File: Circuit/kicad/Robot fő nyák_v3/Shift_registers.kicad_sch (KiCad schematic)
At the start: 2 parts, among them U54 MCP23S17_SO, U55 MCP23S17_SO

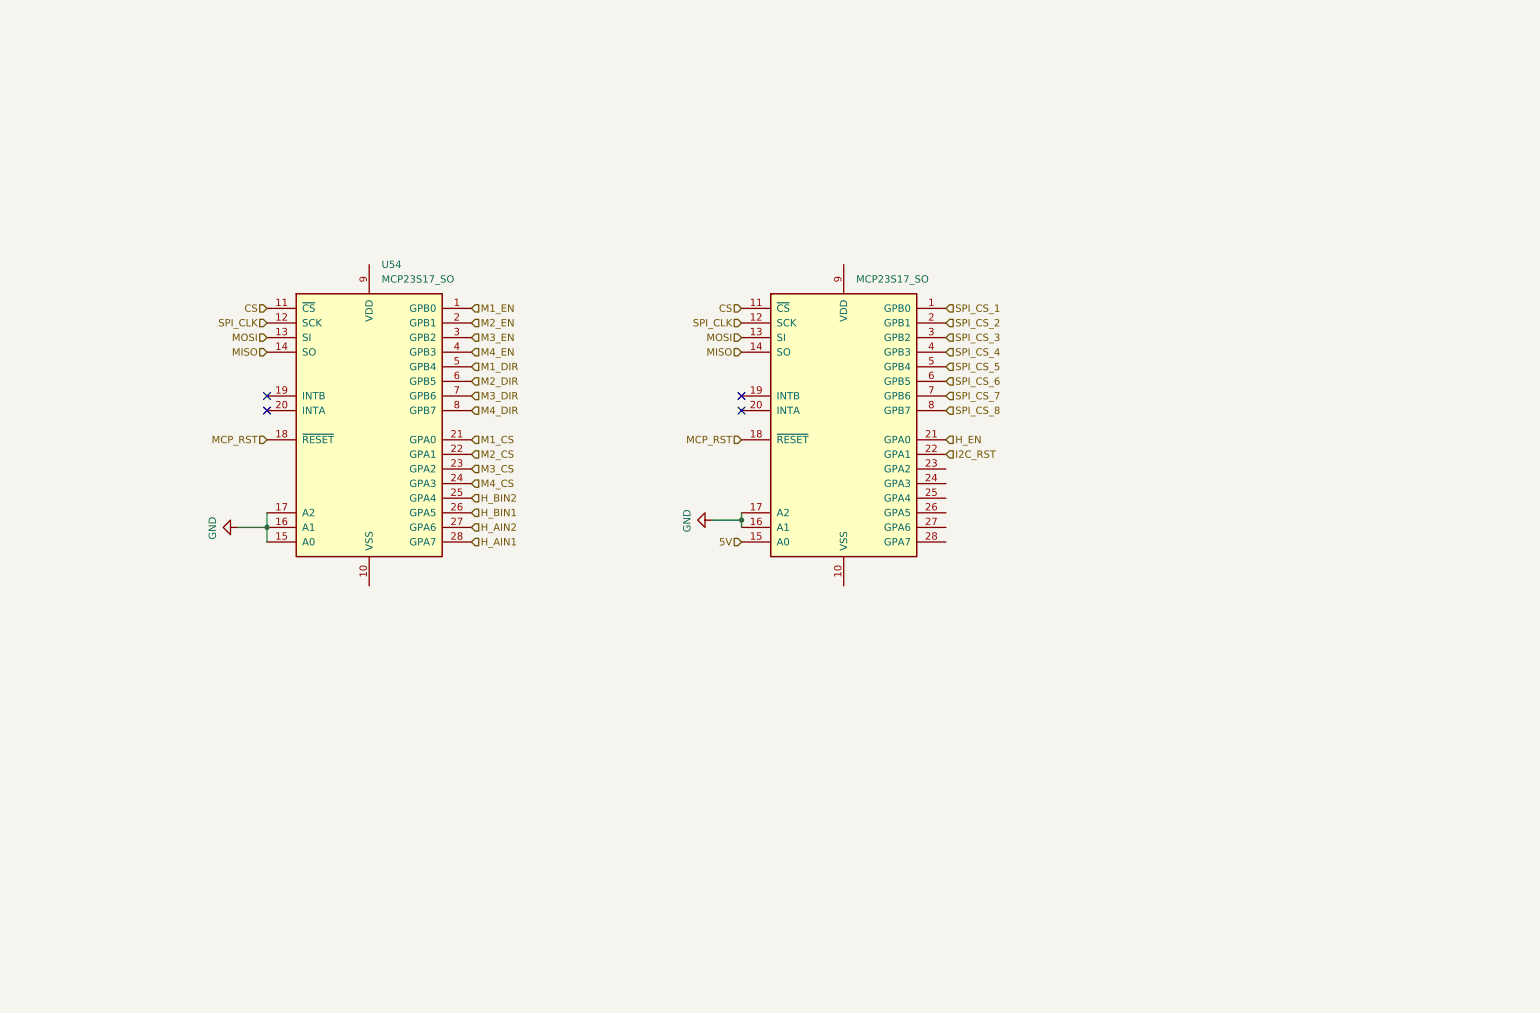
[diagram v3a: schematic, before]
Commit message: kicad  i2c and spi mux fixed and bugfixs
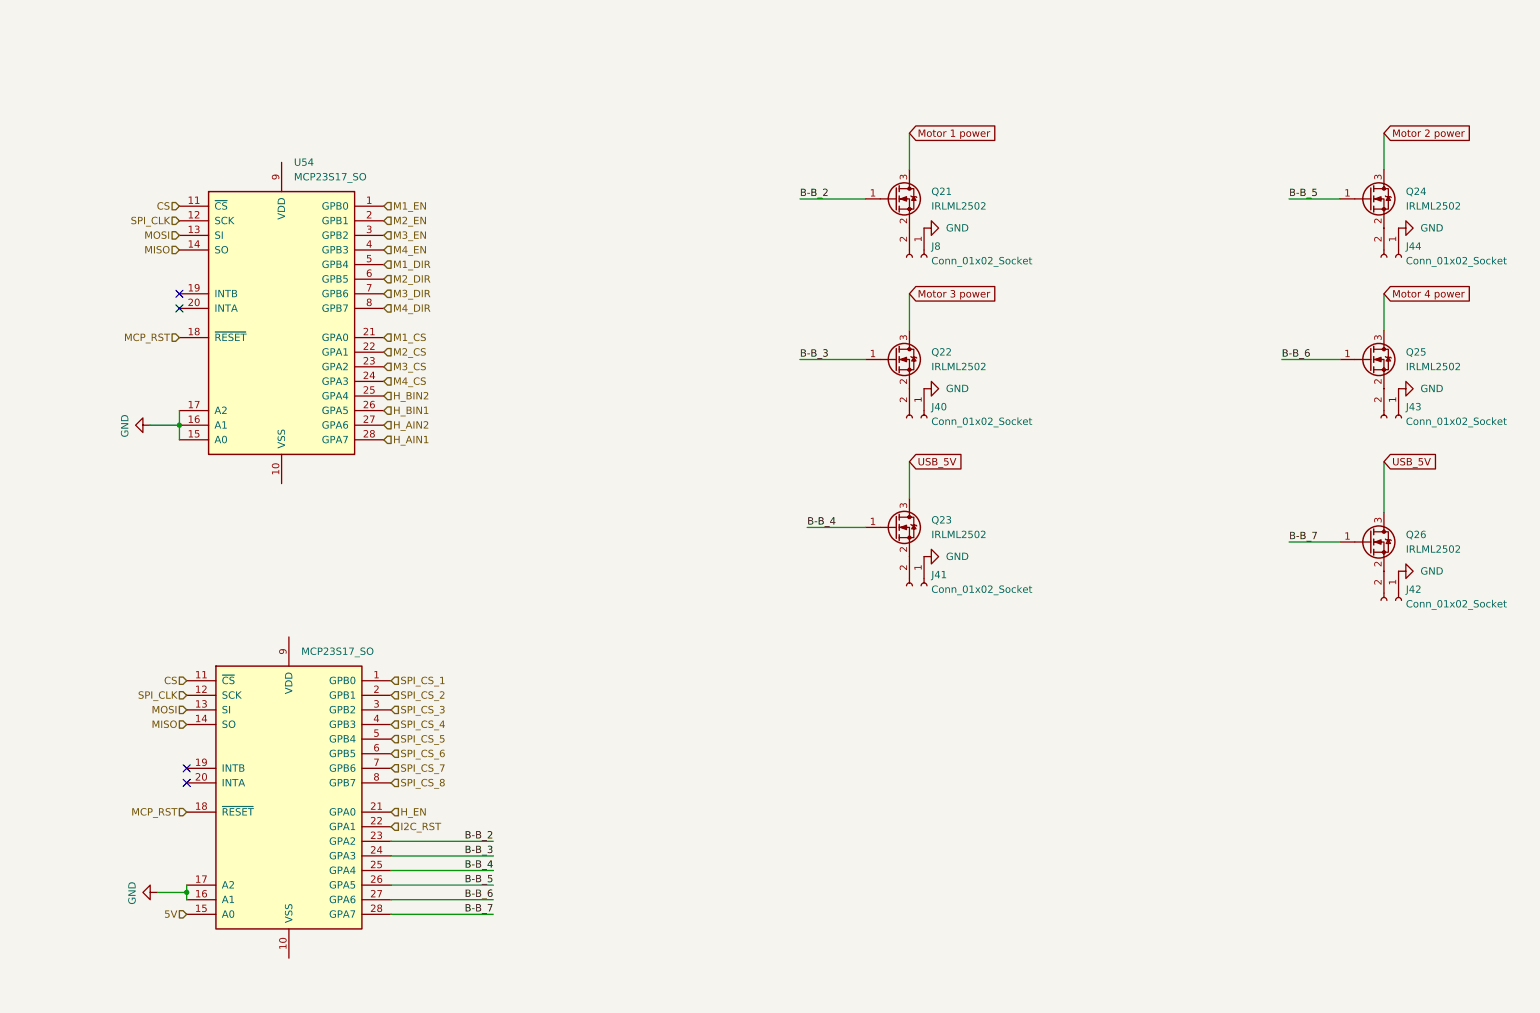
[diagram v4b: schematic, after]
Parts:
- added J40, J41, J42, J43, J44, J8: Conn_01x02_Socket, Connector_JST:JST_PH_B2B-PH-K_1x02_P2.00mm_Vertical, symbol Connector:Conn_01x02_Socket
- added Q21, Q22, Q23, Q24, Q25, Q26: IRLML2502, Package_TO_SOT_SMD:SOT-23, symbol Transistor_FET:IRLML0030
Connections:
- net GND: now also J40.1 (Pin_1), J41.1 (Pin_1), J42.1 (Pin_1), J43.1 (Pin_1), J44.1 (Pin_1), J8.1 (Pin_1)
- net B-B_2: now reaches U55.23 (GPA2)
- net B-B_2: now also Q21.1 (G)
- net B-B_3: now reaches U55.24 (GPA3)
- net B-B_3: now also Q22.1 (G)
- net B-B_4: now reaches U55.25 (GPA4)
- net B-B_4: now also Q23.1 (G)
- net B-B_5: now reaches U55.26 (GPA5)
- net B-B_5: now also Q24.1 (G)
- net B-B_6: now reaches U55.27 (GPA6)
- net B-B_6: now also Q25.1 (G)
- net B-B_7: now reaches U55.28 (GPA7)
- net B-B_7: now also Q26.1 (G)
- new net: J44.2 (Pin_2), Q24.2 (S)
- new net: J41.2 (Pin_2), Q23.2 (S)
- new net: J8.2 (Pin_2), Q21.2 (S)
- new net: J40.2 (Pin_2), Q22.2 (S)
- new net: J42.2 (Pin_2), Q26.2 (S)
- new net: J43.2 (Pin_2), Q25.2 (S)
- new net Motor 1 power: Q21.3 (D)
- new net Motor 2 power: Q24.3 (D)
- new net Motor 3 power: Q22.3 (D)
- new net Motor 4 power: Q25.3 (D)
- new net USB_5V: Q23.3 (D), Q26.3 (D)
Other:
- moved on the sheet: U54

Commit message: kicad update new readme media updates the circuit is 95% finished
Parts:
- added C122, C123, C124: 1uf, symbol Device:C
- added CT7: 10uf, symbol Device:C_Polarized_Small
- U54, U55: footprint Package_SO:SOIC-28W_7.5x17.9mm_P1.27mm -> Package_SO:SSOP-28_3.9x9.9mm_P0.635mm
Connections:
- net 5V: now also C122.1, C123.1, C124.1, CT7.1
- net GND: now also C122.2, C123.2, C124.2, CT7.2

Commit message: readme updated kicad circuit V1
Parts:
- C103: renamed from C122; footprint (none) -> Capacitor_SMD:C_0805_2012Metric
- C104: renamed from C123; footprint (none) -> Capacitor_SMD:C_0805_2012Metric
- C105: renamed from C124; footprint (none) -> Capacitor_SMD:C_0805_2012Metric
- CT6: renamed from CT7; footprint (none) -> Capacitor_Tantalum_SMD:CP_EIA-3528-21_Kemet-B
- renumbered J8 to DC1, J40 to DC2, J41 to DC3, J44 to DC4, J43 to DC5, J42 to DC6, Q21 to Q20, Q22 to Q21, Q23 to Q22, Q24 to Q23, Q25 to Q24, Q26 to Q25, U54 to U53, U55 to U54
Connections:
- net Motor 3 power: no longer names the net of Q21.3 (D)
- net Motor 4 power: no longer names the net of Q24.3 (D)

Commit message: kicad pcb v1.0
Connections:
- net 5V: no longer C103.1, C104.1, C105.1, CT6.1
- net ESP_3v3: now reaches U54.9 (VDD)
- net ESP_3v3: now also C103.1, C104.1, C105.1, CT6.1, Q21.3 (D), Q24.3 (D), U53.9 (VDD)
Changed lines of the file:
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@@
+		)
+	)
+	(global_label "ESP_3v3"
+		(shape input)
+		(at 254 46.99 180)
+		(fields_autoplaced yes)
+		(effects
+			(font
+				(size 1.27 1.27)
+			)
+			(justify right)
+		)
+		(property "Intersheetrefs" "${INTERSHEET_REFS}"
+			(at 242.937 46.99 0)
+			(effects
+				(font
+					(size 1.27 1.27)
+				)
+				(justify right)
+				(hide yes)
+			)
+		)
+	)
+	(global_label "ESP_3v3"
+		(shape input)
+		(at 171.45 46.99 180)
+		(fields_autoplaced yes)
+		(effects
+			(font
+				(size 1.27 1.27)
+			)
+			(justify right)
+		)
+		(property "Intersheetrefs" "${INTERSHEET_REFS}"
+			(at 160.387 46.99 0)
+			(effects
+				(font
+					(size 1.27 1.27)
+				)
+				(justify right)
+				(hide yes)
+			)
 		)
 	)
@@
 		)
 	)
+	(global_label "ESP_3v3"
+		(shape input)
+		(at 63.5 106.68 180)
+		(fields_autoplaced yes)
+		(effects
+			(font
+				(size 1.27 1.27)
+			)
+			(justify right)
+		)
+		(property "Intersheetrefs" "${INTERSHEET_REFS}"
+			(at 52.437 106.68 0)
+			(effects
+				(font
+					(size 1.27 1.27)
+				)
+				(justify right)
+				(hide yes)
+			)
+		)
+	)
+	(global_label "ESP_3v3"
+		(shape input)
+		(at 62.23 24.13 180)
+		(fields_autoplaced yes)
+		(effects
+			(font
+				(size 1.27 1.27)
+			)
+			(justify right)
+		)
+		(property "Intersheetrefs" "${INTERSHEET_REFS}"
+			(at 51.167 24.13 0)
+			(effects
+				(font
+					(size 1.27 1.27)
+				)
+				(justify right)
+				(hide yes)
+			)
+		)
+	)
+	(global_label "ESP_3v3"
+		(shape input)
+		(at 231.14 137.16 180)
+		(fields_autoplaced yes)
+		(effects
+			(font
+				(size 1.27 1.27)
+			)
+			(justify right)
+		)
+		(property "Intersheetrefs" "${INTERSHEET_REFS}"
+			(at 220.077 137.16 0)
+			(effects
+				(font
+					(size 1.27 1.27)
+				)
+				(justify right)
+				(hide yes)
+			)
+		)
+	)
 	(global_label "USB_5V"
 		(shape input)
@@
 		)
 	)
-	(hierarchical_label "5V"
-		(shape input)
-		(at 231.14 137.16 180)
-		(effects
-			(font
-				(size 1.27 1.27)
-			)
-			(justify right)
-		)
-	)
